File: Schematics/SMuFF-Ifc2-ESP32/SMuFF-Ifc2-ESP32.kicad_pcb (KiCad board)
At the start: 2 copper layers, 60.3 x 40 mm, 8 parts, among them J1 DUET/RRF, J2 SMuFF, J3 PanelDue, J4 OLED I2C, J5 Extension, J6 PWR SEL, U1 ESP32-DevKit/NodeMCU

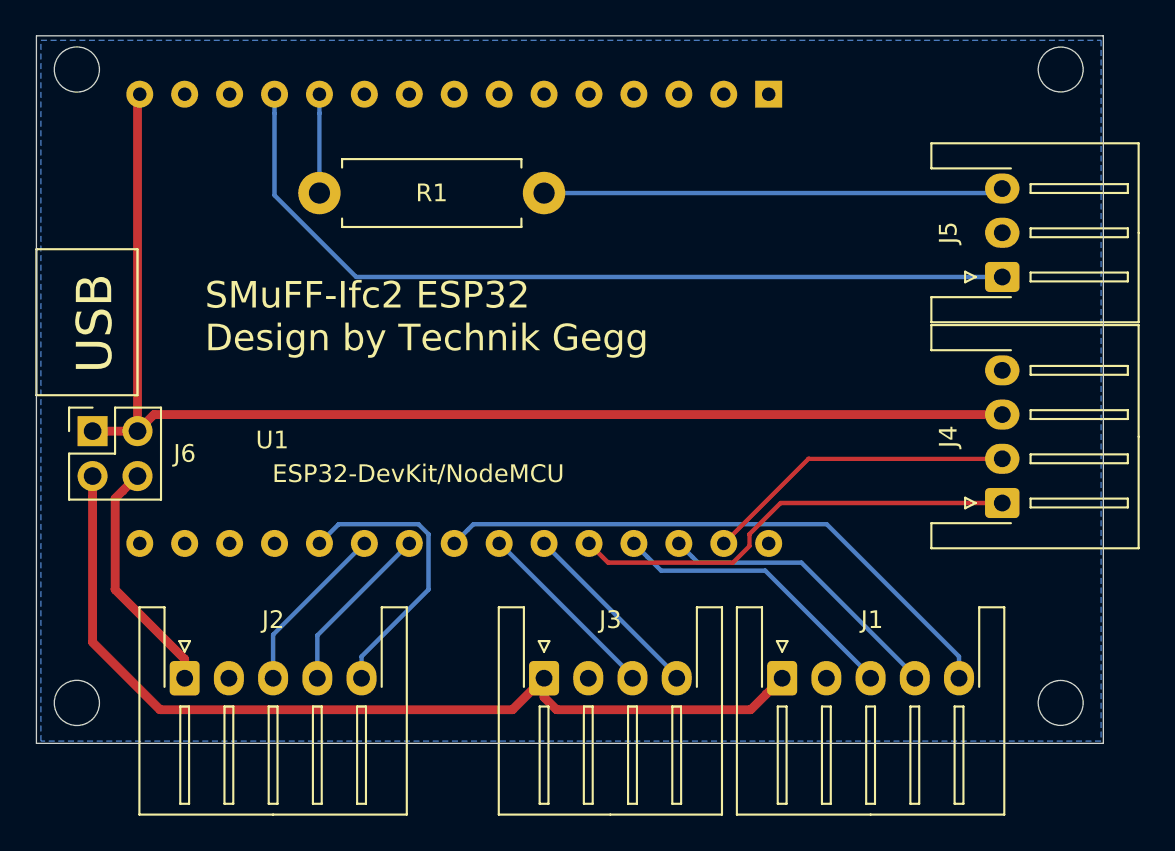
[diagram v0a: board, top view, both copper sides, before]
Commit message: Updated .gitignore
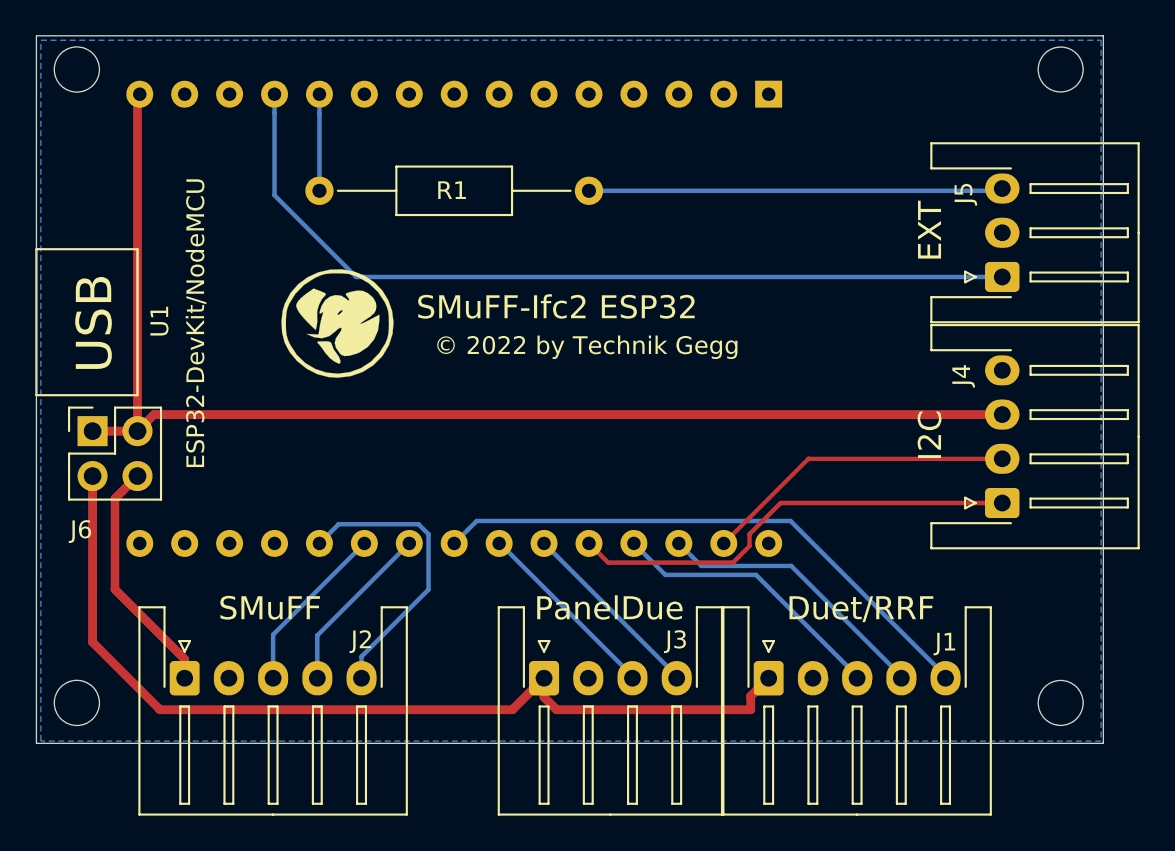
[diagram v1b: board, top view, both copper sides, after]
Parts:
- added G***: LOGO, Symbols:Logo, F.Cu at (119.9, 91.2)
- R1: footprint Resistor_THT:R_Axial_DIN0411_L9.9mm_D3.6mm_P12.70mm_Horizontal -> Resistor_THT:R_Axial_DIN0207_L6.3mm_D2.5mm_P15.24mm_Horizontal
- moved R1 2.54 mm to (134.1, 83.7)
- moved J1 0.76 mm to (144.3, 111.3)
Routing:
- net Net-(J5-Pad3): track 26.0 -> 23.8 mm
- net Net-(J1-Pad5): track 33.3 -> 32.1 mm
- net Net-(J1-Pad4): track 16.7 -> 16.1 mm
- net Net-(J1-Pad3): track 16.7 -> 16.1 mm
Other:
- board text added: "+5V Duet"
- board text added: "+5V SMuFF"
- board text added: "Duet/RRF"
- board text added: "EXT"
- board text added: "I2C"
- board text added: "PanelDue"
- board text added: "SMuFF-Ifc2 ESP32"
- board text added: "© 2022 by Technik Gegg"
- board text removed: "Duet"
- board text removed: "SMuFF-Ifc2 ESP32 Design by Technik Gegg"

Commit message: Updated PCB/Schematics
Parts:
- removed G***: LOGO, Symbols:Logo
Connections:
- J1 pad 2: GND -> Net-(J1-Pad2)
- J1 pad 4: Net-(J1-Pad4) -> GND
- J2 pad 2: GND -> Net-(J2-Pad2)
- J2 pad 4: Net-(J2-Pad4) -> GND
- J3 pad 1: Net-(J1-Pad1) -> Net-(J1-Pad5)
- J6 pad 3: Net-(J1-Pad1) -> Net-(J1-Pad5)
- J6 pad 4: Net-(J2-Pad1) -> Net-(J2-Pad5)
- U1 pad 20: Net-(J2-Pad5) -> Net-(J2-Pad1)
- U1 pad 22: Net-(J2-Pad4) -> Net-(J2-Pad2)
- U1 pad 23: Net-(J1-Pad5) -> Net-(J1-Pad1)
- U1 pad 24: Net-(J3-Pad3) -> Net-(J3-Pad4)
- U1 pad 25: Net-(J3-Pad4) -> Net-(J3-Pad3)
- U1 pad 28: Net-(J1-Pad4) -> Net-(J1-Pad2)
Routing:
- net Net-(J1-Pad5): track 32.1 -> 62.2 mm
- net Net-(J1-Pad1): track 52.5 -> 24.8 mm
- net Net-(J1-Pad4): track 16.1 -> 0.00 mm
- net Net-(J2-Pad2): track 0.00 -> 15.3 mm
- net Net-(J1-Pad2): track 0.00 -> 10.9 mm
- net Net-(J2-Pad4): track 9.90 -> 0.00 mm
- net Net-(J3-Pad4): track 10.7 -> 16.8 mm
- net Net-(J2-Pad5): track 16.7 -> 22.6 mm
- net Net-(J2-Pad1): track 13.6 -> 10.8 mm
- net Net-(J1-Pad3): track 16.1 -> 17.7 mm
- net Net-(J3-Pad3): track 10.8 -> 9.82 mm
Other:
- board text added: "+5V From Duet ►"
- board text added: "+5V From SMuFF ►"
- board text added: "E1STP"
- board text added: "PWR SEL"
- board text added: "REV 2"
- board text removed: "+5V Duet"
- board text removed: "+5V SMuFF"
- board text removed: "E1STOP"

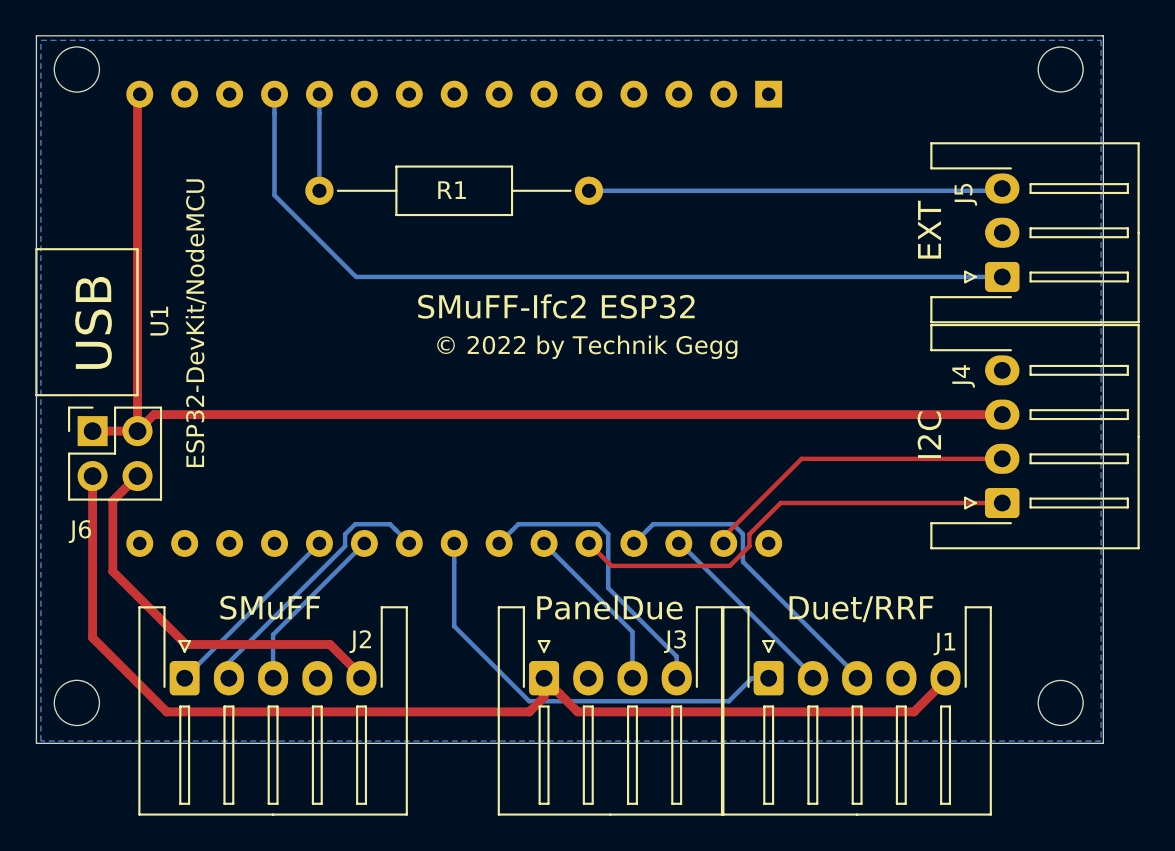
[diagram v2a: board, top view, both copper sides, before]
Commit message: Updated STLs forESP32
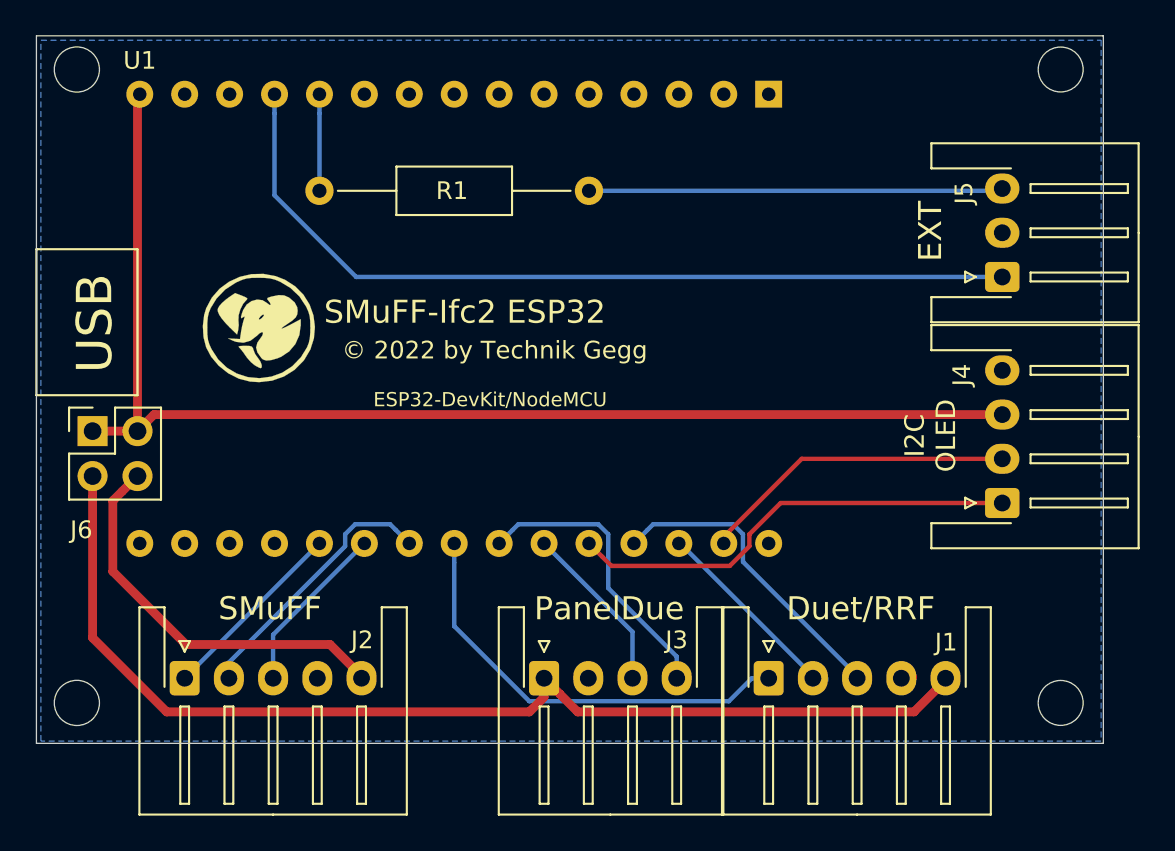
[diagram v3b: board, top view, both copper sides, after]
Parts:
- added G***: LOGO, Symbols:Logo, F.Cu at (115.4, 91.4)
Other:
- board text added: "I2C OLED"
- board text removed: "I2C"
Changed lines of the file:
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@@
     (tracks 88)
     (zones 0)
-    (modules 8)
+    (modules 9)
     (nets 33)
   )
   (page A4)
   (layers
-    (0 F.Cu signal hide)
-    (31 B.Cu signal hide)
+    (0 F.Cu signal)
+    (31 B.Cu signal)
     (32 B.Adhes user hide)
     (33 F.Adhes user hide)
@@
     (44 Edge.Cuts user)
     (45 Margin user)
-    (46 B.CrtYd user)
+    (46 B.CrtYd user hide)
     (47 F.CrtYd user hide)
-    (48 B.Fab user)
+    (48 B.Fab user hide)
     (49 F.Fab user hide)
   )
@@
     (add_net "Net-(U1-Pad9)")
   )
+  (module Symbols:Logo (layer F.Cu)
+    (at 115.443 91.44)
+    (fp_text reference G*** (at 0 0) (layer F.SilkS) hide
+      (effects (font (size 1.524 1.524) (thickness 0.3)))
+    )
+    (fp_text value LOGO (at 0.75 0) (layer F.SilkS) hide
+      (effects (font (size 1.524 1.524) (thickness 0.3)))
+    )
+    (fp_poly (pts (xy -0.952972 -1.81693) (xy -0.72891 -1.721715) (xy -0.644729 -1.652262) (xy -0.677637 -1.587313)
+      (xy -0.693549 -1.574961) (xy -0.882716 -1.359714) (xy -1.040773 -1.047417) (xy -1.13874 -0.710341)
+      (xy -1.150235 -0.436075) (xy -1.135104 -0.148543) (xy -1.163609 0.119558) (xy -1.165383 0.127)
+      (xy -1.227667 0.381) (xy -1.665079 -0.042333) (xy -1.908134 -0.297856) (xy -2.11627 -0.552338)
+      (xy -2.238655 -0.740643) (xy -2.322468 -0.937551) (xy -2.319973 -1.074145) (xy -2.232865 -1.23227)
+      (xy -2.079298 -1.407292) (xy -1.847998 -1.609311) (xy -1.71584 -1.706975) (xy -1.340768 -1.965031)
+      (xy -0.952972 -1.81693)) (layer F.SilkS) (width 0.01))
+    (fp_poly (pts (xy 1.441807 -1.831698) (xy 1.711177 -1.710197) (xy 1.715823 -1.707148) (xy 2.020692 -1.448014)
+      (xy 2.1732 -1.163291) (xy 2.19864 -0.968682) (xy 2.175202 -0.755063) (xy 2.080296 -0.578204)
+      (xy 1.884669 -0.39995) (xy 1.629833 -0.226775) (xy 1.384691 -0.061442) (xy 1.284638 0.026647)
+      (xy 1.323578 0.036515) (xy 1.495413 -0.032816) (xy 1.794048 -0.182323) (xy 1.820333 -0.196235)
+      (xy 2.370667 -0.488463) (xy 2.370667 -0.148221) (xy 2.292505 0.412664) (xy 2.070382 0.914756)
+      (xy 1.72284 1.331618) (xy 1.26842 1.636812) (xy 1.058703 1.722443) (xy 0.680947 1.830737)
+      (xy 0.415701 1.85216) (xy 0.22995 1.786425) (xy 0.151002 1.7145) (xy -0.078337 1.391109)
+      (xy -0.154323 1.107127) (xy -0.079669 0.836265) (xy 0.042333 0.661893) (xy 0.200563 0.432656)
+      (xy 0.241571 0.285752) (xy 0.18023 0.241613) (xy 0.031414 0.32067) (xy -0.109876 0.452788)
+      (xy -0.469549 0.729326) (xy -0.869619 0.8433) (xy -1.295961 0.791964) (xy -1.481667 0.71941)
+      (xy -1.735667 0.599791) (xy -1.399854 0.617396) (xy -1.064042 0.635) (xy -1.003827 0.226685)
+      (xy -0.947616 -0.079599) (xy -0.878374 -0.361202) (xy -0.853918 -0.438925) (xy -0.839942 -0.484511)
+      (xy 0 -0.484511) (xy 0.051475 -0.46855) (xy 0.169852 -0.550803) (xy 0.28084 -0.675979)
+      (xy 0.298898 -0.745324) (xy 0.211444 -0.735393) (xy 0.093113 -0.643146) (xy 0.009254 -0.525603)
+      (xy 0 -0.484511) (xy -0.839942 -0.484511) (xy -0.80294 -0.605197) (xy -0.821699 -0.640225)
+      (xy -0.890112 -0.591744) (xy -0.990614 -0.538965) (xy -1.009616 -0.619022) (xy -0.946954 -0.837953)
+      (xy -0.878508 -1.017534) (xy -0.685888 -1.315377) (xy -0.411281 -1.513109) (xy -0.096745 -1.598771)
+      (xy 0.215661 -1.560405) (xy 0.469515 -1.400848) (xy 0.616432 -1.287567) (xy 0.676415 -1.30088)
+      (xy 0.634661 -1.414175) (xy 0.542716 -1.532417) (xy 0.470557 -1.63118) (xy 0.503499 -1.693627)
+      (xy 0.668089 -1.753068) (xy 0.733216 -1.771445) (xy 1.132443 -1.851026) (xy 1.441807 -1.831698)) (layer F.SilkS) (width 0.01))
+    (fp_poly (pts (xy -0.531078 1.024162) (xy -0.393134 1.060091) (xy -0.32776 1.149577) (xy -0.300088 1.252904)
+      (xy -0.20504 1.480982) (xy -0.046695 1.706856) (xy -0.039361 1.714876) (xy 0.088078 1.897582)
+      (xy 0.161723 2.087872) (xy 0.168462 2.234195) (xy 0.105833 2.285684) (xy -0.001925 2.245047)
+      (xy -0.186894 2.145144) (xy -0.229445 2.119656) (xy -0.441684 1.945522) (xy -0.659974 1.699608)
+      (xy -0.737367 1.590805) (xy -0.89981 1.358583) (xy -1.046352 1.177915) (xy -1.100589 1.124526)
+      (xy -1.146678 1.06402) (xy -1.078245 1.031777) (xy -0.871218 1.019596) (xy -0.789894 1.018693)
+      (xy -0.531078 1.024162)) (layer F.SilkS) (width 0.01))
+    (fp_poly (pts (xy 0.952894 -2.922794) (xy 1.479422 -2.716756) (xy 2.063936 -2.341804) (xy 2.531047 -1.864339)
+      (xy 2.875328 -1.308155) (xy 3.091353 -0.697047) (xy 3.173693 -0.054808) (xy 3.116921 0.594767)
+      (xy 2.915612 1.227884) (xy 2.564338 1.820749) (xy 2.525716 1.870643) (xy 2.019558 2.379332)
+      (xy 1.420199 2.754375) (xy 0.747709 2.987996) (xy 0.022162 3.072417) (xy -0.493243 3.04037)
+      (xy -1.132272 2.87479) (xy -1.734932 2.567317) (xy -2.268614 2.143401) (xy -2.700709 1.628489)
+      (xy -2.978776 1.100667) (xy -3.125784 0.530378) (xy -3.157505 0) (xy -2.913599 0)
+      (xy -2.906258 0.386806) (xy -2.873934 0.66988) (xy -2.803486 0.91441) (xy -2.681769 1.185585)
+      (xy -2.66965 1.209927) (xy -2.291415 1.789235) (xy -1.808081 2.250391) (xy -1.242907 2.585688)
+      (xy -0.619152 2.787419) (xy 0.039925 2.847877) (xy 0.711065 2.759355) (xy 1.329043 2.534932)
+      (xy 1.895808 2.168086) (xy 2.375625 1.670925) (xy 2.718214 1.118985) (xy 2.823677 0.861563)
+      (xy 2.884138 0.58976) (xy 2.910152 0.243125) (xy 2.913599 0) (xy 2.906257 -0.386805)
+      (xy 2.873934 -0.66988) (xy 2.803486 -0.91441) (xy 2.681769 -1.185584) (xy 2.66965 -1.209927)
+      (xy 2.294077 -1.777129) (xy 1.789381 -2.254195) (xy 1.200162 -2.607045) (xy 0.912399 -2.724476)
+      (xy 0.640047 -2.792463) (xy 0.316615 -2.823238) (xy -0.007923 -2.829269) (xy -0.391242 -2.822622)
+      (xy -0.673004 -2.791813) (xy -0.920704 -2.722459) (xy -1.201834 -2.600173) (xy -1.294633 -2.555031)
+      (xy -1.897283 -2.166036) (xy -2.391463 -1.651355) (xy -2.718214 -1.118984) (xy -2.823677 -0.861563)
+      (xy -2.884138 -0.589759) (xy -2.910152 -0.243125) (xy -2.913599 0) (xy -3.157505 0)
+      (xy -3.163432 -0.099093) (xy -3.09172 -0.717647) (xy -2.978776 -1.100666) (xy -2.656999 -1.706465)
+      (xy -2.216714 -2.211071) (xy -1.681049 -2.606101) (xy -1.073129 -2.883171) (xy -0.41608 -3.033899)
+      (xy 0.266969 -3.049901) (xy 0.952894 -2.922794)) (layer F.SilkS) (width 0.01))
+  )
   (module Resistor_THT:R_Axial_DIN0207_L6.3mm_D2.5mm_P15.24mm_Horizontal (layer F.Cu)
     (at 134.112 83.693 180)
@@
     (descr "ESPWROOM32, ESP32, 30 GPIOs version")
     (attr virtual)
-    (fp_text reference U1 (at 0.127 34.417 90) (layer F.SilkS)
-      (effects (font (size 1 1) (thickness 0.15)))
-    )
-    (fp_text value ESP32-DevKit/NodeMCU (at 0.254 32.385 270) (layer F.SilkS)
-      (effects (font (size 1 1) (thickness 0.15)))
+    (fp_text reference U1 (at -14.605 35.56) (layer F.SilkS)
+      (effects (font (size 1 1) (thickness 0.15)))
+    )
+    (fp_text value ESP32-DevKit/NodeMCU (at 4.572 15.748) (layer F.SilkS)
+      (effects (font (size 0.8 0.8) (thickness 0.15)))
     )
     (fp_arc (start 12 43.46) (end 12 45.46) (angle -90) (layer Dwgs.User) (width 0.12))
@@
     (effects (font (size 1 1) (thickness 0.15)) (justify mirror))
   )
-  (gr_text "© 2022 by Technik Gegg" (at 133.985 92.456) (layer F.SilkS)
+  (gr_text "© 2022 by Technik Gegg" (at 128.778 92.71) (layer F.SilkS)
     (effects (font (size 1 1) (thickness 0.15)))
   )
@@
     (effects (font (size 1.3 1.3) (thickness 0.25)))
   )
-  (gr_text I2C (at 153.416 97.536 90) (layer F.SilkS)
-    (effects (font (size 1.3 1.3) (thickness 0.25)))
+  (gr_text "I2C\nOLED" (at 153.416 97.536 90) (layer F.SilkS)
+    (effects (font (size 1.1 1.1) (thickness 0.25)))
   )
   (gr_text Duet/RRF (at 149.479 107.315) (layer F.SilkS)
@@
     (effects (font (size 2 2) (thickness 0.2)))
   )
-  (gr_text "SMuFF-Ifc2 ESP32" (at 124.333 90.297) (layer F.SilkS)
+  (gr_text "SMuFF-Ifc2 ESP32" (at 119.126 90.551) (layer F.SilkS)
     (effects (font (size 1.3 1.3) (thickness 0.25)) (justify left))
   )

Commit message: Updated to 1.1.2; See README.md
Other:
- net class Default removed
- rule pad_to_mask_clearance: 0.051 -> 0
